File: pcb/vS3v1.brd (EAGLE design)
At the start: 49.8 x 69.6 mm, 102 parts, among them IC1 DS3231/SO, J1 BM04B-SRSS-TB(LF)(SN), J10 48099-4000, J11 SIM8060-6-0-14-00-A, J12 S8411-45R, J13 MEM2067-02-180-00-A_REVB, J2 BM04B-SRSS-TB(LF)(SN), J3 BM04B-SRSS-TB(LF)(SN), J4 BM04B-SRSS-TB(LF)(SN), J5 BM04B-SRSS-TB(LF)(SN)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

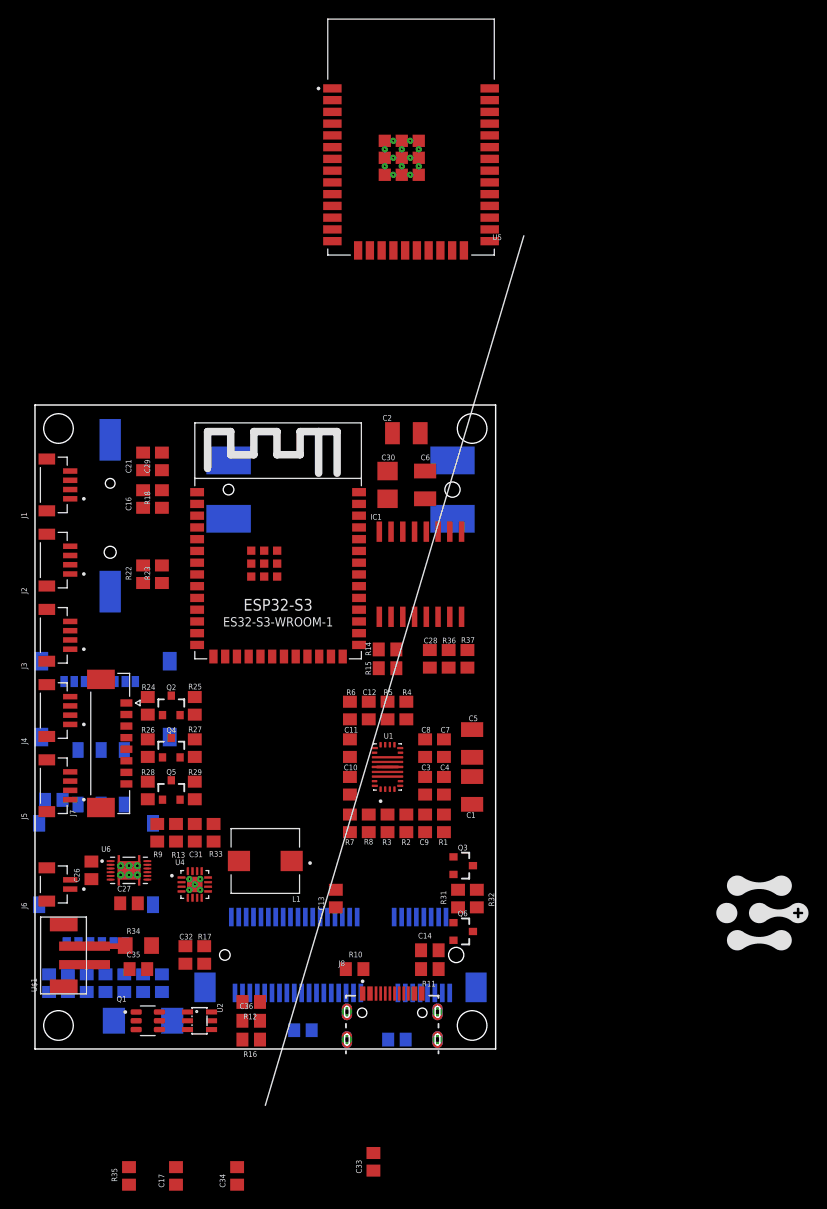
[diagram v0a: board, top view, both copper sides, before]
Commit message: feat: Add initial PCB design, schematic, and datasheet for miniMadre.
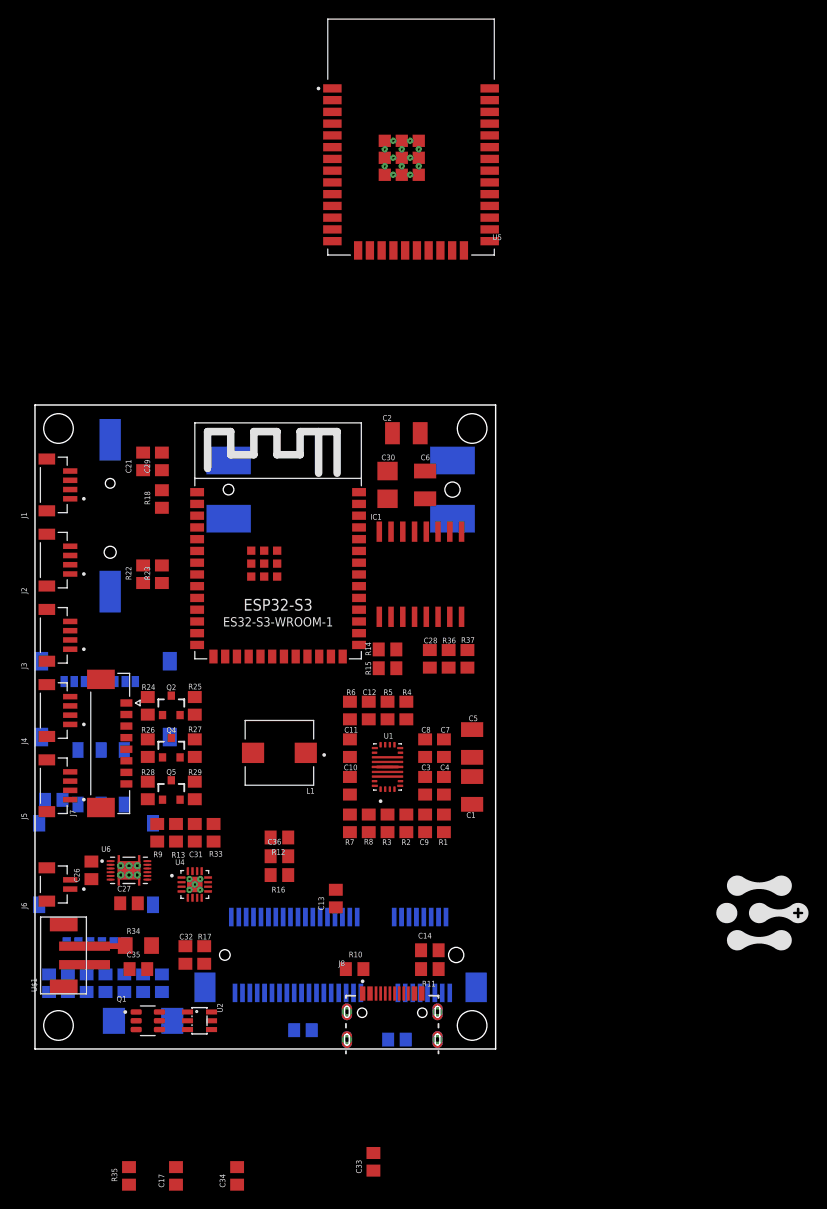
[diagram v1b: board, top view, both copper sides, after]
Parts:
- removed C16: 10uF, rcl:C0805
- removed Q3, Q6: 5.8A/30V/35mΩ, transistor:SOT23-3
- removed R31, R32: 470R, rcl:R0805
- moved C36 18.0 mm to (-12.2, 33.5)
- moved R12 18.0 mm to (-12.2, 35.6)
- moved R16 18.0 mm to (-12.2, 31.5)
- moved L1 11.8 mm to (-12.2, 44.7)
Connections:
- removed net !DTR: Q3.2, R31.2
- removed net !RTS: Q6.2, R32.2
- removed net N$25: Q6.1, R31.1
- removed net N$26: Q3.1, R32.1
- net BOOT: no longer Q3.3
- net GND: no longer C16.2
- net RST: no longer C16.1, Q6.3
